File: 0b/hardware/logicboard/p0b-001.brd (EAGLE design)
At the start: 70 x 41 mm, 24 parts, among them IC1 7404D, IC4 LTC485S, IC5 LTC485S, J0 DC5V, J7 DIN5, J9 DIN5, X7 NELTRON-7810-XPXC

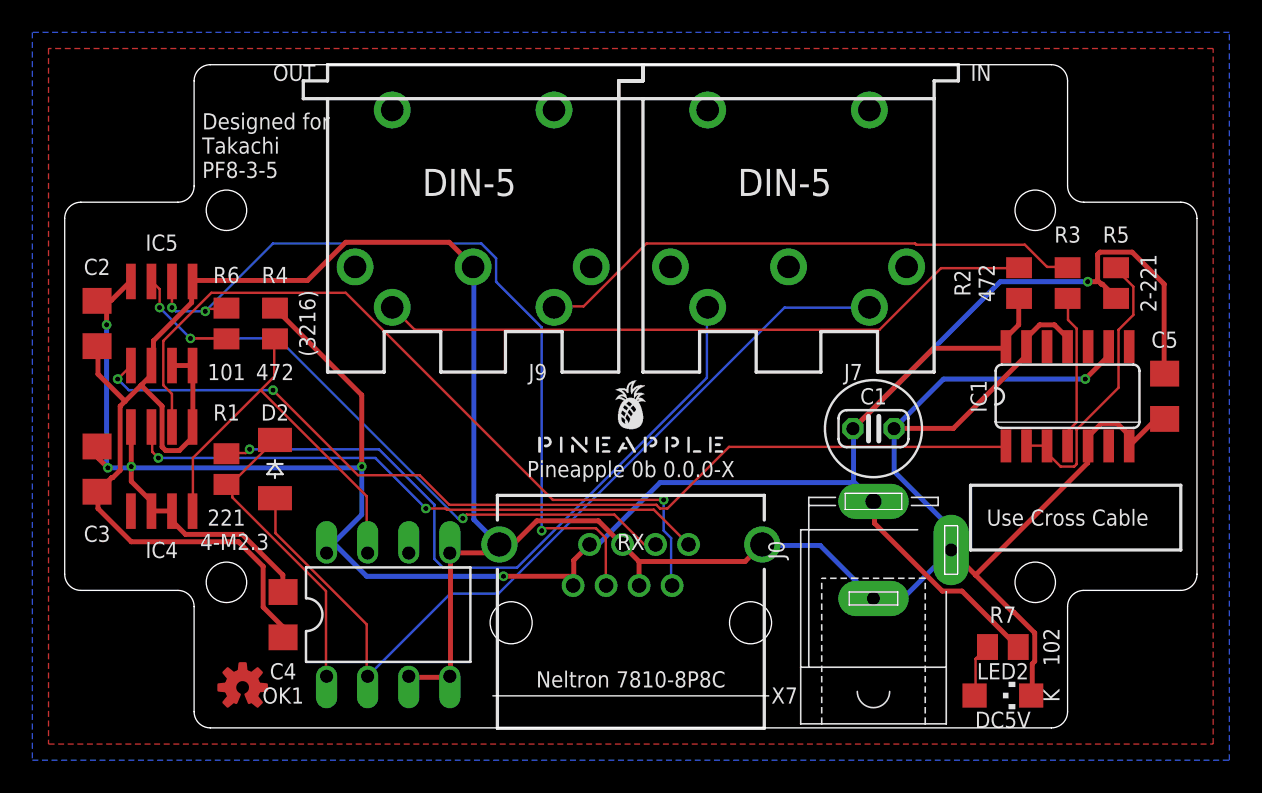
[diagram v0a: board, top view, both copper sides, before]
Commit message: Now runs by 7805 regulator.
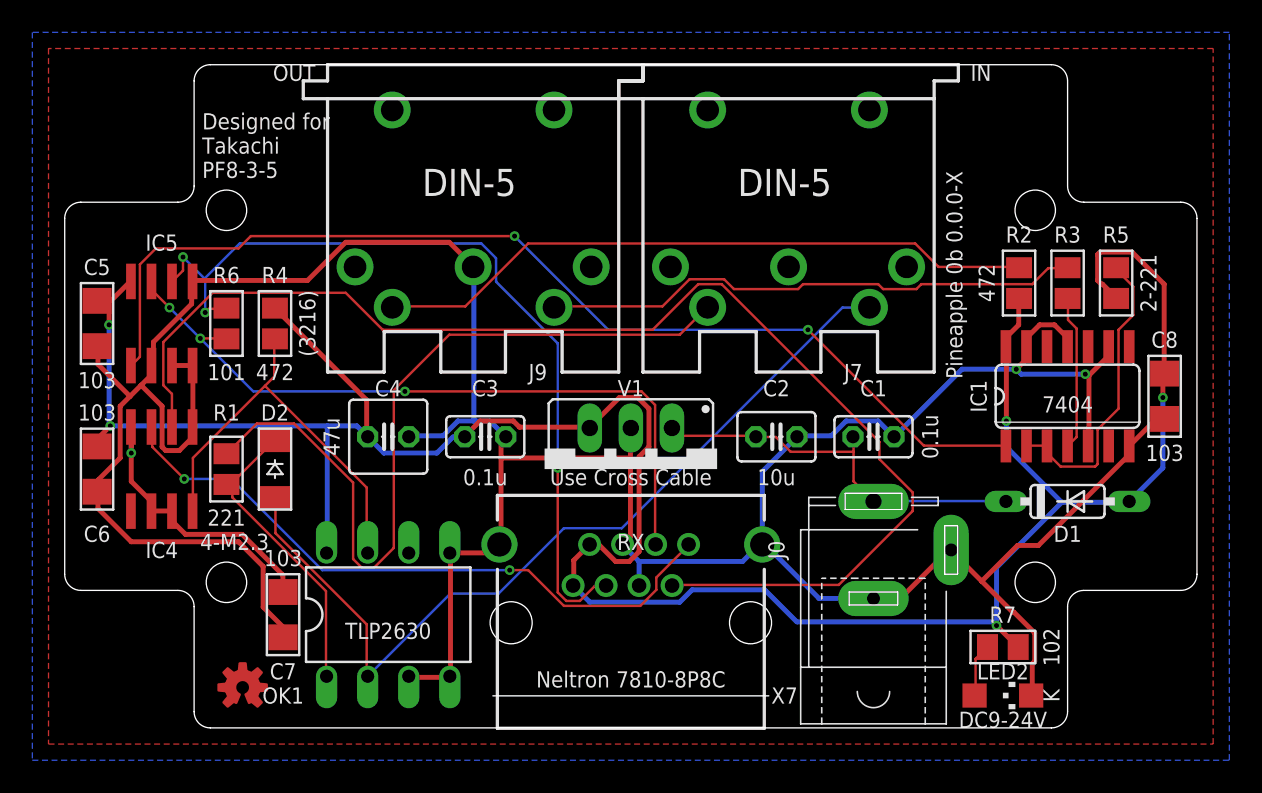
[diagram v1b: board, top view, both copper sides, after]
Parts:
- added C6, C7, C8: 103, rcl:C1206
- added D1: 1N4148DO35-7, diode:DO35-7
- added V1: 5V, v-reg:78XXS
- C1: value 100n -> 0.1u; device rcl:C025-024X044 -> rcl:C025-025X050
- C2: value (none) -> 10u; device rcl:C1206 -> rcl:C025-030X050
- C3: value (none) -> 0.1u; device rcl:C1206 -> rcl:C025-025X050
- C4: value (none) -> 47u; device rcl:C1206 -> rcl:C025-050X050
- C5: value (none) -> 103
- R1, R2, R3: value 220 -> 221
- R4, R5: value 220 -> 472
- R6: value 220 -> 101
- moved C5 66.2 mm to (2.00, 25.0)
- moved C2 42.6 mm to (44.0, 18.0), turned to 0 degrees
- moved C3 24.1 mm to (26.0, 18.0), turned to 0 degrees
- moved U$1 15.0 mm to (35.0, 32.0), flipped to the bottom
- moved C4 12.8 mm to (20.0, 18.0), turned to 0 degrees
- moved C1 0.50 mm to (50.0, 18.0)
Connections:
- new net VIN: C1.1, C2.1, D1.C, J0.3, V1.IN
- net GND: now also C6.2, C7.2, C8.2, V1.GND
- net VCC: now also C6.1, C7.1, C8.1, D1.A, V1.OUT; no longer C1.1, C2.1, J0.3
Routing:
- net TX+: track 48.5 -> 79.1 mm, vias 1 -> 0
- net VIN: track 0.00 -> 24.6 mm
- net VCC: track 169.8 -> 181.6 mm
- net GND: track 203.4 -> 213.9 mm, vias 1 -> 2
- net MISND: track 44.1 -> 49.4 mm, vias 1 -> 0
- net RX: track 61.0 -> 66.1 mm
- net RX-: track 41.0 -> 44.9 mm
- net TX-: track 37.1 -> 40.5 mm
- net RX+: track 50.5 -> 52.4 mm
- net NMIDIOUT: track 18.0 -> 18.8 mm
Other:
- board text added: "0.1u"
- board text added: "103"
- board text added: "10u"
- board text added: "47u"
- board text added: "7404"
- board text added: "DC9-24V"
- board text added: "TLP2630"
- board text removed: "DC5V"

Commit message: Fixed pinout of 0b.
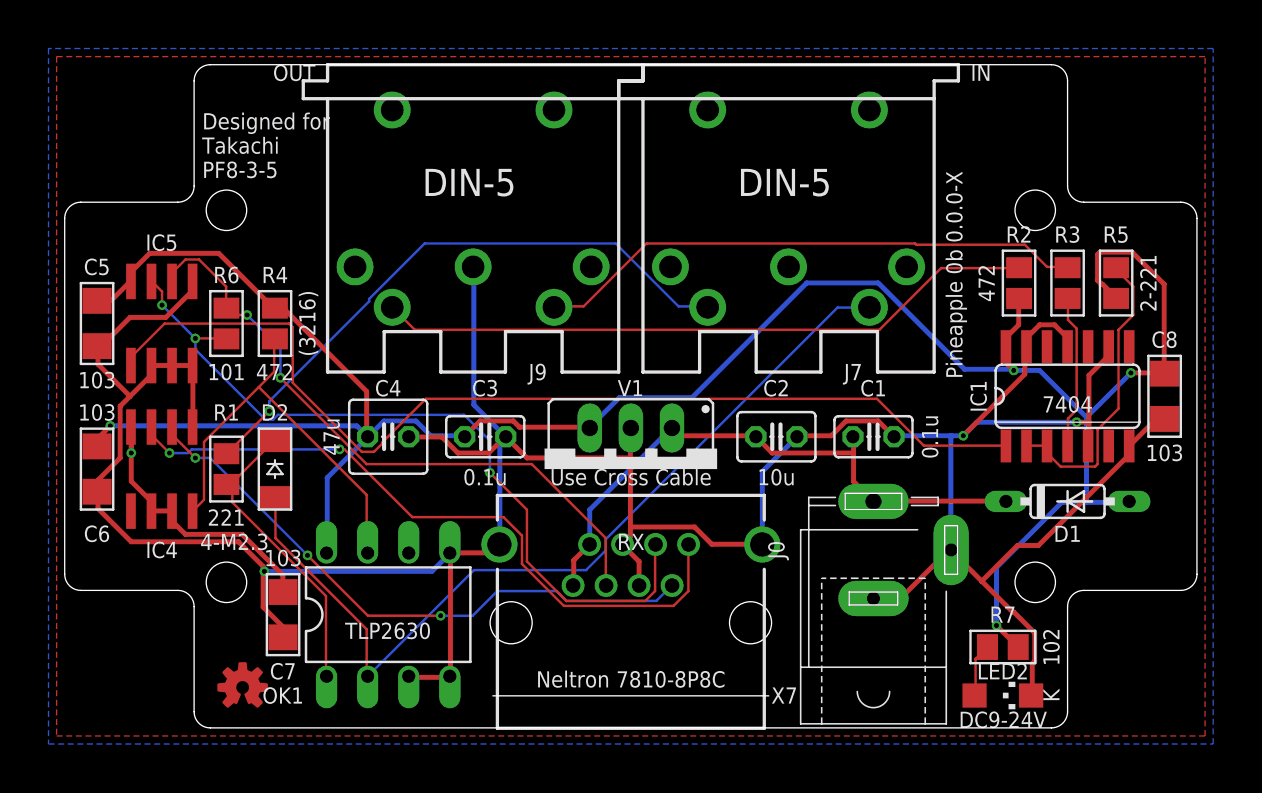
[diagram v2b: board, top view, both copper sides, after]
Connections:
- net VCC: no longer X7.7, X7.8
- net VIN: now also X7.7, X7.8
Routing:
- net TX+: track 79.1 -> 37.3 mm, vias 0 -> 3
- net VCC: track 181.6 -> 167.6 mm, vias 6 -> 5
- net RX+: track 52.4 -> 39.6 mm, vias 3 -> 2
- net VIN: track 24.6 -> 36.9 mm
- net MISND: track 49.4 -> 37.2 mm, vias 0 -> 1
- net GND: track 213.9 -> 207.9 mm, vias 2 -> 3
- net RX-: track 44.9 -> 48.6 mm
- net RX: track 66.1 -> 63.4 mm, vias 2 -> 0
- net TX-: track 40.5 -> 42.6 mm

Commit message: MIDI Phantom.
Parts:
- added S1: MIDIPHANTOM, switch-dil:DIP04YL
- OK1: value HCPL2630 -> HCPL0600; device optocoupler:DIL08 -> optocoupler:SOIC08
- moved OK1 12.4 mm to (11.5, 16.0)
- moved D2 9.71 mm to (22.5, 14.0), turned to 0 degrees
- moved C7 9.22 mm to (15.5, 16.0)
- moved R1 8.00 mm to (18.0, 16.0)
- moved C1 7.00 mm to (43.0, 18.0)
- moved C2 4.50 mm to (48.5, 18.0)
- moved C4 1.50 mm to (21.5, 18.0)
- moved C3 1.00 mm to (27.0, 18.0)
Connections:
- removed net VIN: C1.1, C2.1, D1.C, J0.3, V1.IN, X7.7, X7.8
- new net MIDIINGND: J7.1, S1.1
- new net MIDIINV+: J7.3, S1.2
- new net MIDIOUTGND: J9.1, S1.3
- new net MIDIOUTV+: J9.3, S1.4
- new net V+: C1.1, C2.1, D1.C, J0.3, S1.5, S1.7, V1.IN, X7.7, X7.8
- net GND: now also S1.6, S1.8; no longer OK1.3, OK1.4
- net MIDIIN: now also OK1.2; no longer OK1.1
- net MIRTN: now also OK1.3; no longer OK1.2
- net TX: now also OK1.6; no longer OK1.7
- net VCC: now also OK1.7
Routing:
- net V+: track 0.00 -> 52.0 mm
- net MIDIINV+: track 0.00 -> 49.8 mm
- net MIDIINGND: track 0.00 -> 49.0 mm
- net VIN: track 36.9 -> 0.00 mm
- net MIDIOUTV+: track 0.00 -> 33.9 mm
- net MIDIOUTGND: track 0.00 -> 27.8 mm
- net RX: track 63.4 -> 89.5 mm
- net VCC: track 167.6 -> 146.0 mm, vias 5 -> 11
- net TX: track 25.8 -> 12.8 mm
- net MISND: track 37.2 -> 25.6 mm, vias 1 -> 0
- net RX-: track 48.6 -> 59.0 mm, vias 3 -> 0
- net MIDIIN: track 18.8 -> 12.1 mm
- net NMIDIOUT: track 18.8 -> 16.2 mm
- net GND: track 207.9 -> 210.2 mm, vias 3 -> 5
- net TX-: track 42.6 -> 44.3 mm, vias 2 -> 0
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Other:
- board text added: "0600"
- board text added: "HCPL"
- board text added: "MIDI PHANTOM"
- board text removed: "TLP2630"
